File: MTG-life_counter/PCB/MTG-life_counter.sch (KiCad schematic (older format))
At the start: 38 parts, among them J2 AVR-ISP-6, Q1 IRLML6244, Q2 Si2301DS, Q3 Si2301DS, SW1 SW_Push, SW2 SW_Push, U2 AT90S4433-8P, U3 HDSP-H101, U4 HDSP-H101, Y1 8 MHz

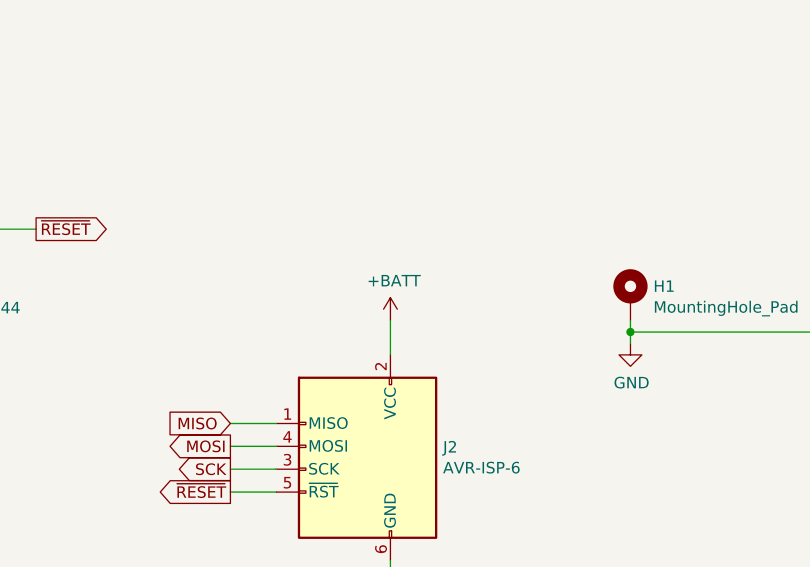
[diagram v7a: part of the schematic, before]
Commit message: Add a diode as a cheap voltage dropper.
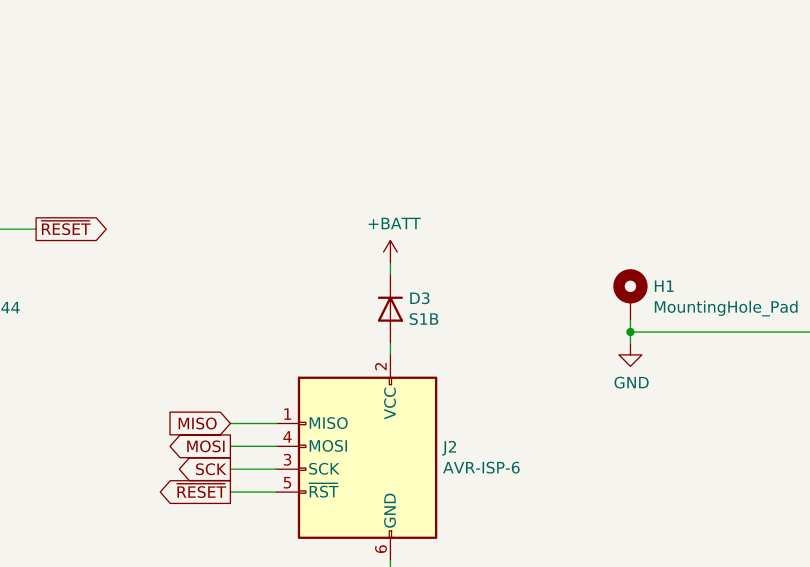
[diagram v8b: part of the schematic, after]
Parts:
- added D3: S1B, Diode_SMD:D_SMA_Handsoldering, symbol Device:D
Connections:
- net +BATT: now also D3.1 (K); no longer J2.2 (VCC)
- new net: D3.2 (A), J2.2 (VCC)
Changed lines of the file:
@@
 L power:+BATT #PWR05
 U 1 1 61C19A2C
-P 6200 6200
-F 0 "#PWR05" H 6200 6050 50  0001 C CNN
-F 1 "+BATT" H 6215 6373 50  0000 C CNN
-F 2 "" H 6200 6200 50  0001 C CNN
-F 3 "" H 6200 6200 50  0001 C CNN
-	1    6200 6200
+P 6200 5950
+F 0 "#PWR05" H 6200 5800 50  0001 C CNN
+F 1 "+BATT" H 6215 6123 50  0000 C CNN
+F 2 "" H 6200 5950 50  0001 C CNN
+F 3 "" H 6200 5950 50  0001 C CNN
+	1    6200 5950
 	1    0    0    -1
 $EndComp
@@
 $EndComp
 NoConn ~ 4100 2650
-Wire Wire Line
-	6200 6200 6200 6350
+$Comp
+L Device:D D3
+U 1 1 638FCA74
+P 6200 6150
+F 0 "D3" V 6154 6230 50  0000 L CNN
+F 1 "S1B" V 6245 6230 50  0000 L CNN
+F 2 "Diode_SMD:D_SMA_Handsoldering" H 6200 6150 50  0001 C CNN
+F 3 "~" H 6200 6150 50  0001 C CNN
+	1    6200 6150
+	0    1    1    0
+$EndComp
+Wire Wire Line
+	6200 6350 6200 6300
+Wire Wire Line
+	6200 6000 6200 5950
 Wire Bus Line
 	5250 3150 5250 4250
